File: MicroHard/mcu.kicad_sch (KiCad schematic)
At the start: 28 parts, among them J2 GPIO_header, J3 MCU_Debug, J4 Micro_SD_Card_Det2, J5 Controller Connector, SW1 KMR221NGLFS, SW2 KMR221NGLFS, SW3 KMR221NGLFS, U3 EFM32GG842F1024, Y1 48MHz

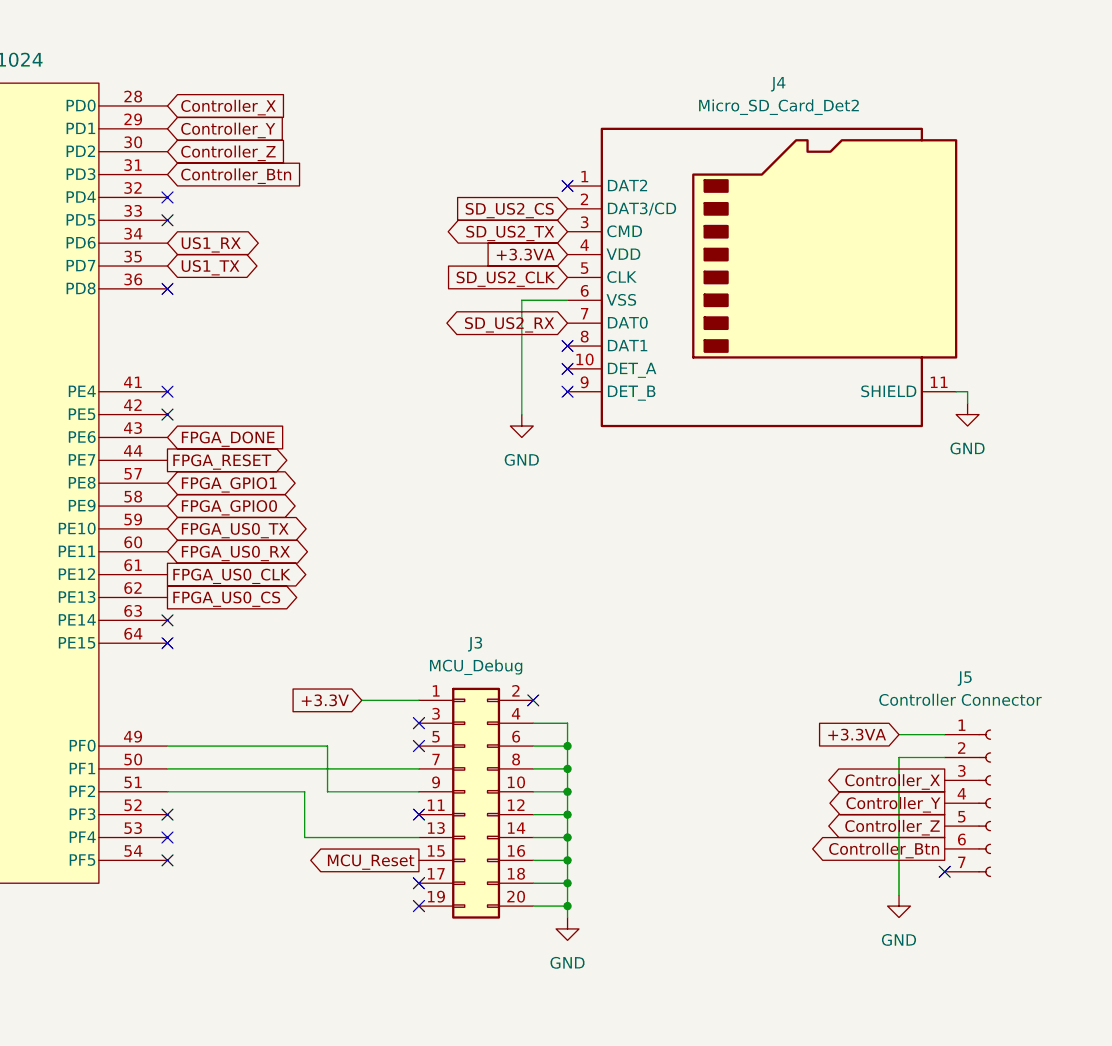
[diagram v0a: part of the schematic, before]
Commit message: Add Controller Btn 2 to MCU
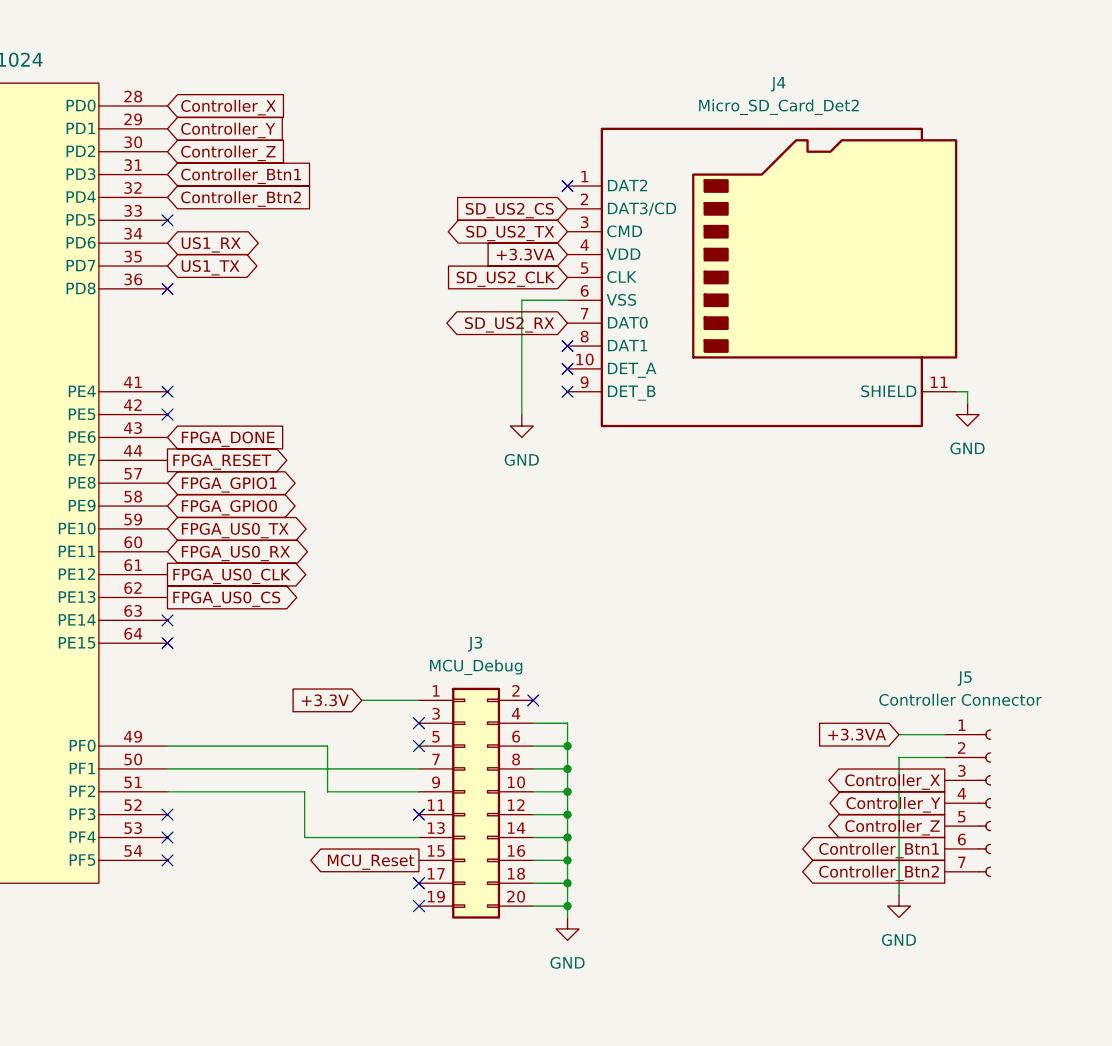
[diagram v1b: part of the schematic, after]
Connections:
- net Controller_Btn2: now reaches U3.32 (PD4)
- net Controller_Btn2: now also J5.7 (Pin_7)
- net Controller_Btn renamed Controller_Btn1
- no-connect marks 32 -> 30
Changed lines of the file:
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@@
 	)
 	(no_connect
-		(at 175.26 39.37)
-	)
-	(no_connect
 		(at 175.26 110.49)
 	)
@@
 	)
 	(no_connect
-		(at 261.62 114.3)
-	)
-	(no_connect
 		(at 175.26 41.91)
 	)
@@
 		)
 	)
+	(global_label "Controller_Btn2"
+		(shape input)
+		(at 175.26 39.37 0)
+		(fields_autoplaced yes)
+		(effects
+			(font
+				(size 1.27 1.27)
+			)
+			(justify left)
+		)
+		(property "Intersheetrefs" "${INTERSHEET_REFS}"
+			(at 193.0011 39.37 0)
+			(effects
+				(font
+					(size 1.27 1.27)
+				)
+				(justify left)
+				(hide yes)
+			)
+		)
+	)
 	(global_label "Controller_Y"
 		(shape output)
@@
 		)
 	)
+	(global_label "Controller_Btn2"
+		(shape output)
+		(at 261.62 114.3 180)
+		(fields_autoplaced yes)
+		(effects
+			(font
+				(size 1.27 1.27)
+			)
+			(justify right)
+		)
+		(property "Intersheetrefs" "${INTERSHEET_REFS}"
+			(at 243.8789 114.3 0)
+			(effects
+				(font
+					(size 1.27 1.27)
+				)
+				(justify right)
+				(hide yes)
+			)
+		)
+	)
 	(global_label "+3.3V"
 		(shape input)
@@
 		)
 	)
-	(global_label "Controller_Btn"
+	(global_label "Controller_Btn1"
 		(shape input)
 		(at 175.26 36.83 0)
@@
 		)
 		(property "Intersheetrefs" "${INTERSHEET_REFS}"
-			(at 191.7916 36.83 0)
+			(at 193.0011 36.83 0)
 			(effects
 				(font
@@
 		)
 	)
-	(global_label "Controller_Btn"
+	(global_label "Controller_Btn1"
 		(shape output)
 		(at 261.62 111.76 180)
@@
 		)
 		(property "Intersheetrefs" "${INTERSHEET_REFS}"
-			(at 245.0884 111.76 0)
+			(at 243.8789 111.76 0)
 			(effects
 				(font
